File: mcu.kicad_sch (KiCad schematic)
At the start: 1 part

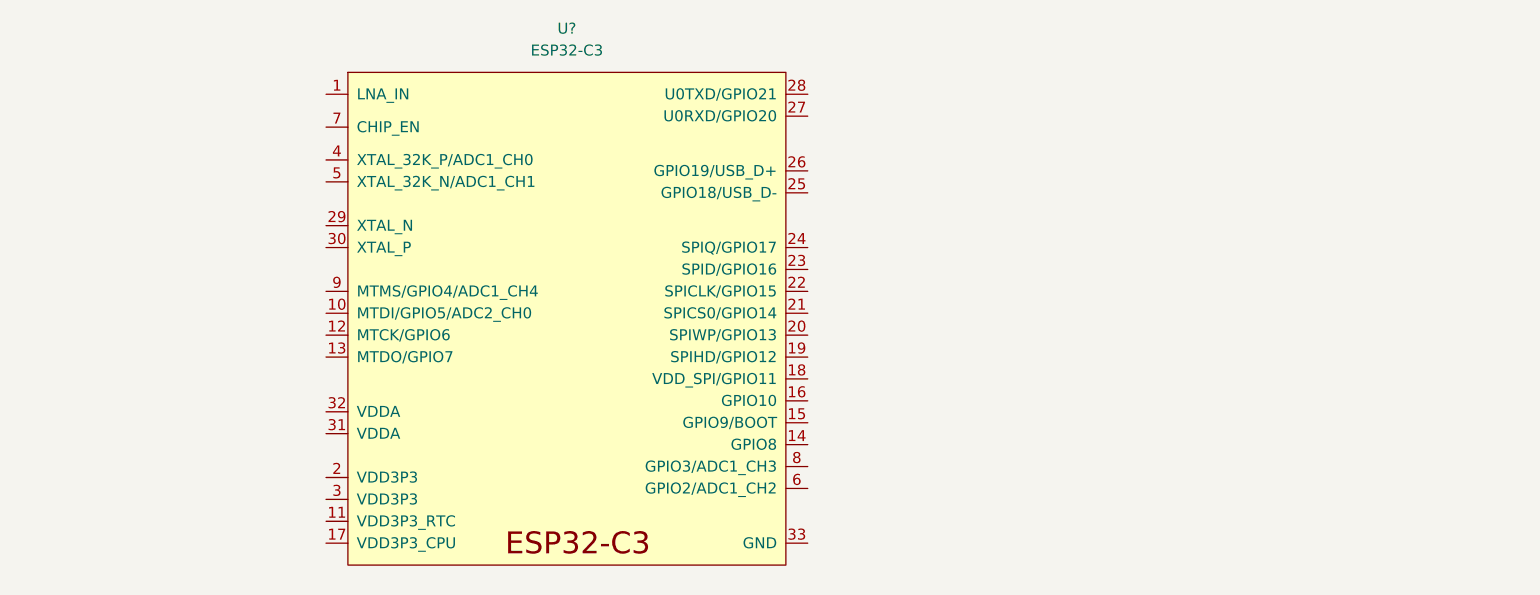
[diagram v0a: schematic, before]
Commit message: Add Flash memory Feat: - Add flash memory circuit
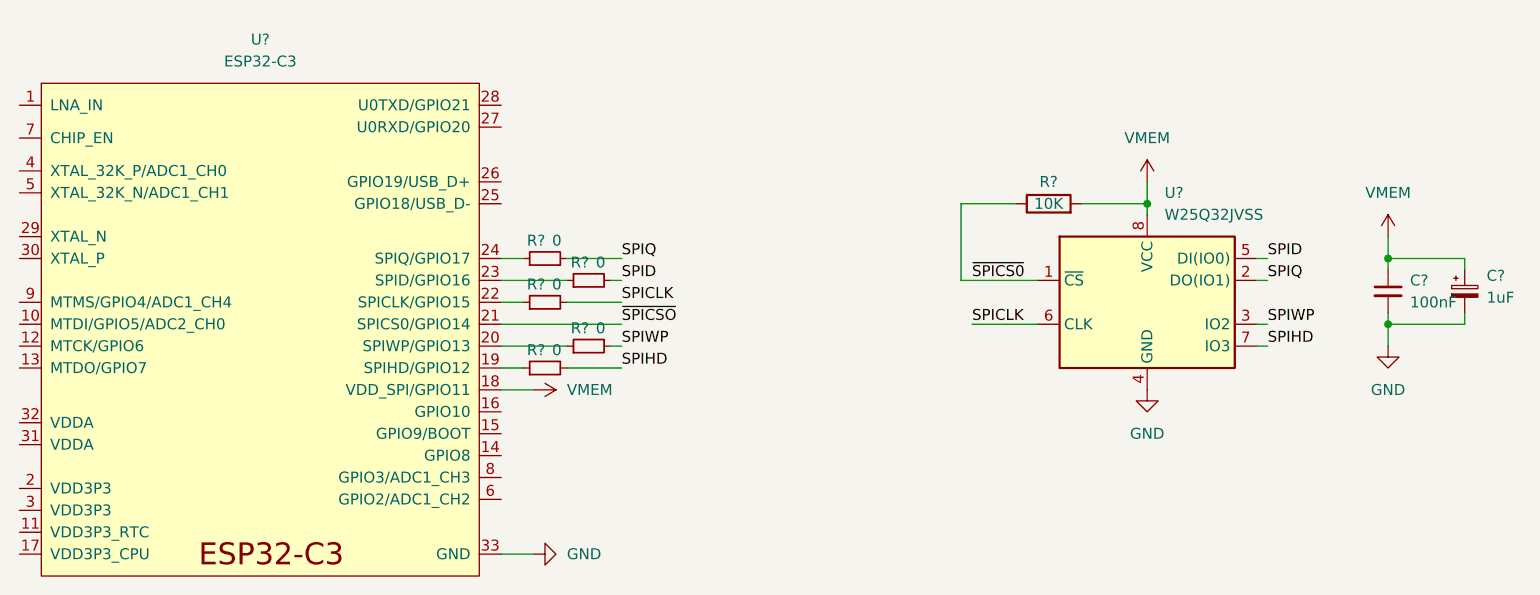
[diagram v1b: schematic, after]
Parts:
- added C?: 1uF, symbol Device:C_Polarized_Small
- added C?: 100nF, symbol Device:C_Small
- added R?: 10K, symbol Device:R
- added R? (x5): 0, Resistor_SMD:R_0603_1608Metric_Pad0.98x0.95mm_HandSolder, symbol Device:R_Small
- added U?: W25Q32JVSS, Package_SO:SOIC-8_5.23x5.23mm_P1.27mm, symbol Memory_Flash:W25Q32JVSS
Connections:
- net VMEM: now reaches U?.18 (VDD_SPI/GPIO11)
- net VMEM: now also C?.1, C?.1, R?.2, U?.8 (VCC)
- net at U?.19 (SPIHD/GPIO12): now also R?.1
- net at U?.20 (SPIWP/GPIO13): now also R?.1
- net ~{SPICSO}: now reaches U?.21 (SPICS0/GPIO14)
- net at U?.22 (SPICLK/GPIO15): now also R?.1
- net at U?.23 (SPID/GPIO16): now also R?.1
- net at U?.24 (SPIQ/GPIO17): now also R?.1
- net GND: now reaches U?.33 (GND)
- net GND: now also C?.2, C?.2, U?.4 (GND)
- new net SPICLK: R?.2, U?.6 (CLK)
- new net SPID: R?.2, U?.5 (DI(IO0))
- new net SPIHD: R?.2, U?.7 (IO3)
- new net SPIQ: R?.2, U?.2 (DO(IO1))
- new net SPIWP: R?.2, U?.3 (IO2)
- new net ~{SPICS0}: R?.1, U?.1 (~{CS})
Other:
- moved on the sheet: U?
